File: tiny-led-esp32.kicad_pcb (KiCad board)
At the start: 2 copper layers, 28.6 x 52.7 mm, 38 parts, among them J1 USB_B_Micro, U1 AMS1117-3.3, U2 ESP32-WROOM-32

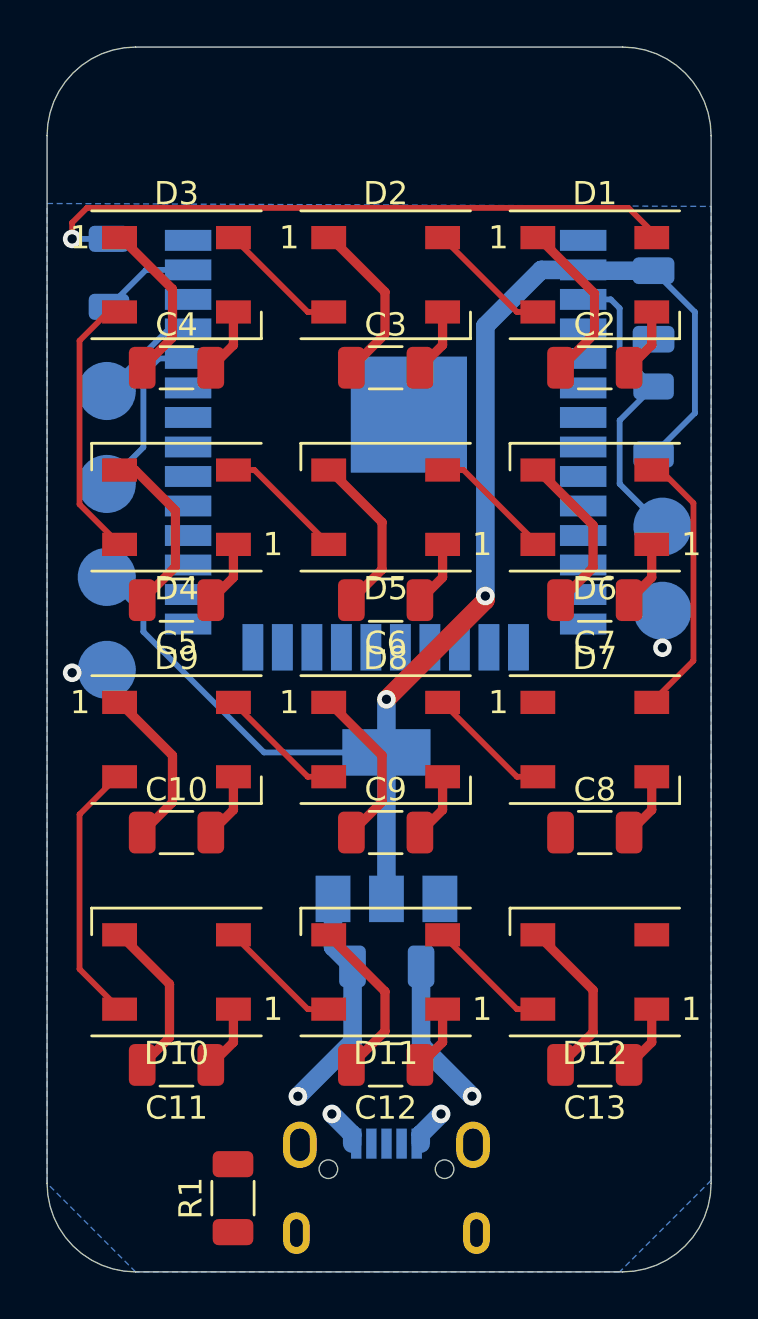
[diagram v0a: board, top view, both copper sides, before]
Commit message: added mount holes, inner layers
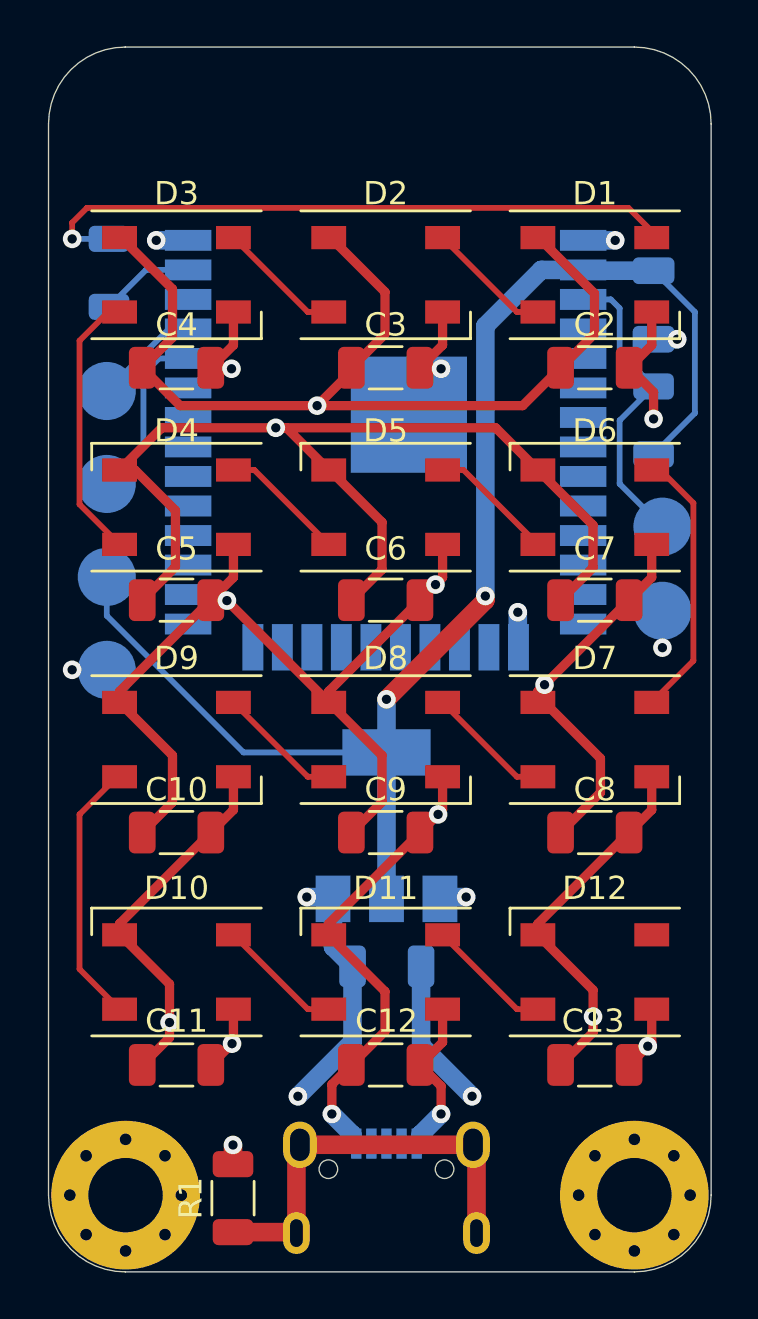
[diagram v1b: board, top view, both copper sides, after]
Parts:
- added H1: GND, MountingHole:MountingHole_3.2mm_M3_Pad_Via, F.Cu at (141.8, 125.6)
- added H2: 5V, MountingHole:MountingHole_3.2mm_M3_Pad_Via, F.Cu at (163.7, 125.6)
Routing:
- net +5V: track 64.3 -> 122.1 mm, vias 2 -> 9
- net GND: track 69.8 -> 126.1 mm, vias 3 -> 17
- net Net-(J1-Pad6): track 0.00 -> 17.9 mm
- net +3V3: track 59.7 -> 60.2 mm
- net (no net): vias 1 -> 0
- added copper zone on In2.Cu, net +5V
- added copper zone on In1.Cu, net GND
- removed copper zone on B.Cu, net GND
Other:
- board size 28.6 x 52.7 mm -> 28.5 x 52.7 mm
- copper layers 2 -> 4

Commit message: finished with v0.1
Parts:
- added TP7: TestPoint, TestPoint:TestPoint_Pad_D2.5mm, B.Cu at (141.0, 91.0)
- moved R3 6.27 mm to (164.5, 86.0), turned to 90 degrees
- moved TP3 4.00 mm to (141.0, 99.0)
- moved TP4 4.00 mm to (141.0, 95.0)
- moved TP5 4.00 mm to (141.0, 103.0)
- moved TP6 4.00 mm to (141.0, 107.0)
- moved C1 3.97 mm to (164.5, 91.3)
- moved TP1 1.88 mm to (164.5, 95.0)
- moved TP2 1.51 mm to (164.5, 99.0)
- moved R1 0.32 mm to (146.7, 125.7)
- moved R2 0.08 mm to (141.1, 86.0)
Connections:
- net Net-(R3-Pad1) renamed EN
- U2 pad 25: Net-(U2-Pad25) -> IO0
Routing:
- net IO0: track 0.00 -> 15.0 mm
- net TX: track 4.61 -> 9.68 mm
- net +3V3: track 60.2 -> 55.3 mm
- net RX: track 7.58 -> 11.3 mm
- net GND: track 126.1 -> 128.4 mm
- net +5V: track 122.1 -> 123.2 mm, vias 9 -> 8
- net EN: track 13.1 -> 12.0 mm
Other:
- board text added: "3v3"
- board text added: "EN"
- board text added: "GND"
- board text added: "IO0"
- board text added: "JLCJLCJLCJLC"
- board text added: "RX"
- board text added: "TX"
- board text added: "github.com: brushknight/tiny-led-esp32"
- board text added: "tiny-led-esp32@v0.1"
